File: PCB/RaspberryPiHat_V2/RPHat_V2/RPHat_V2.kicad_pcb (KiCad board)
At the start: 4 copper layers, 109.9 x 66.8 mm, 60 parts, among them IC1 TXB0108DQSR, J1 Raspberry_Pi_2_3, J11 Conn_01x03, J12 Conn_01x03, J13 Conn_01x03, J14 Conn_01x03, J15 Conn_01x01, J16 Conn_01x06, J2 Hall effect connector Right, J3 Halleffect Connector Left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

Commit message: Commit update
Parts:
- removed C13: 100nF, Capacitor_SMD:C_0603_1608Metric_Pad1.08x0.95mm_HandSolder
- removed J4: Conn_01x03, Connector_PinHeader_2.54mm:PinHeader_1x03_P2.54mm_Vertical
- removed R9: 100k, Resistor_SMD:R_0603_1608Metric_Pad0.98x0.95mm_HandSolder
- removed U5: AH1806-P, Connector_PinHeader_2.54mm:PinHeader_1x03_P2.54mm_Vertical
- BT1: footprint Connector_AMASS:AMASS_XT60-F_1x02_P7.20mm_Vertical -> Connector_AMASS:AMASS_XT60-M_1x02_P7.20mm_Vertical
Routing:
- net +3V3: track 134.3 -> 124.3 mm
- net OUTPUT: track 7.26 -> 0.00 mm
- net +5V: track 177.1 -> 170.6 mm
- net SCL: track 79.4 -> 81.7 mm
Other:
- board size 109.9 x 66.8 mm -> 75.4 x 66.8 mm

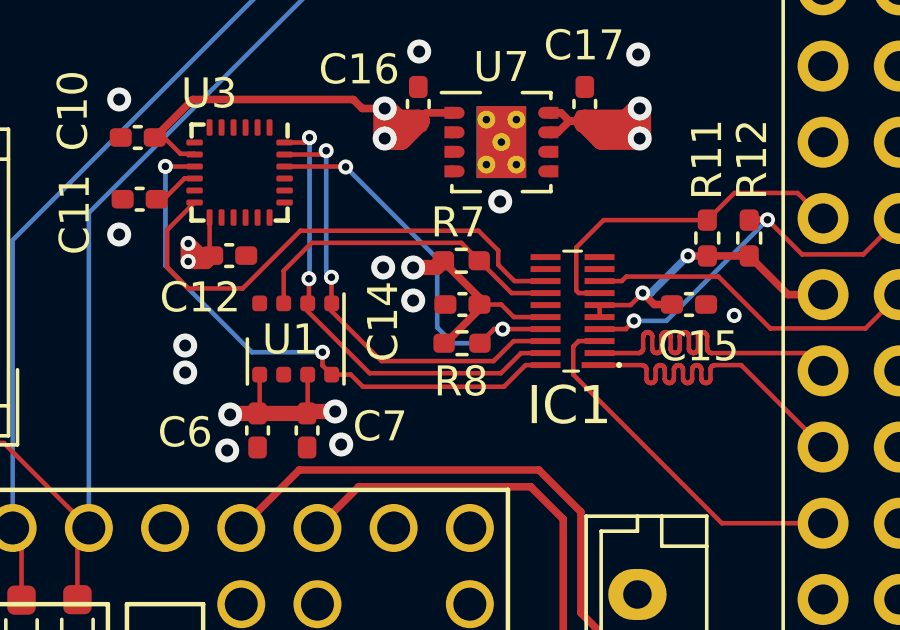
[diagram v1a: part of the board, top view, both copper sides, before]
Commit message: Fixed linking issue and finished pcb
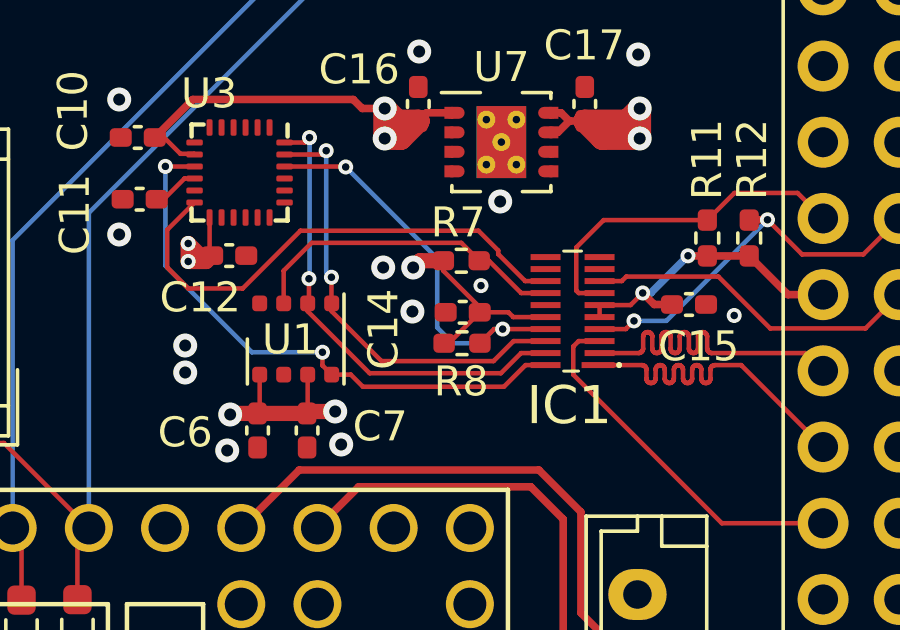
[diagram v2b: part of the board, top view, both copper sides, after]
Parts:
- moved C14 0.26 mm to (150.9, 112.3)
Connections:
- IC1 pad 15: Net-(IC1-Pad15) -> GNDREF
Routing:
- net GNDREF: vias 37 -> 38
